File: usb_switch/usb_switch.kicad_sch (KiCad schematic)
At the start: 79 parts, among them J1 Jack-DC, J2 USB_B_Micro, J3 Conn_01x04, J4 USB_A, J5 USB_A, J6 USB_A, J7 USB_A, J8 UART, U1 AMS1117-3.3, U2 USB2514B_Bi, U3 MIC2026-1BM, U4 MIC2026-1BM, U5 MCP2221-I_SL, Y1 24MHz

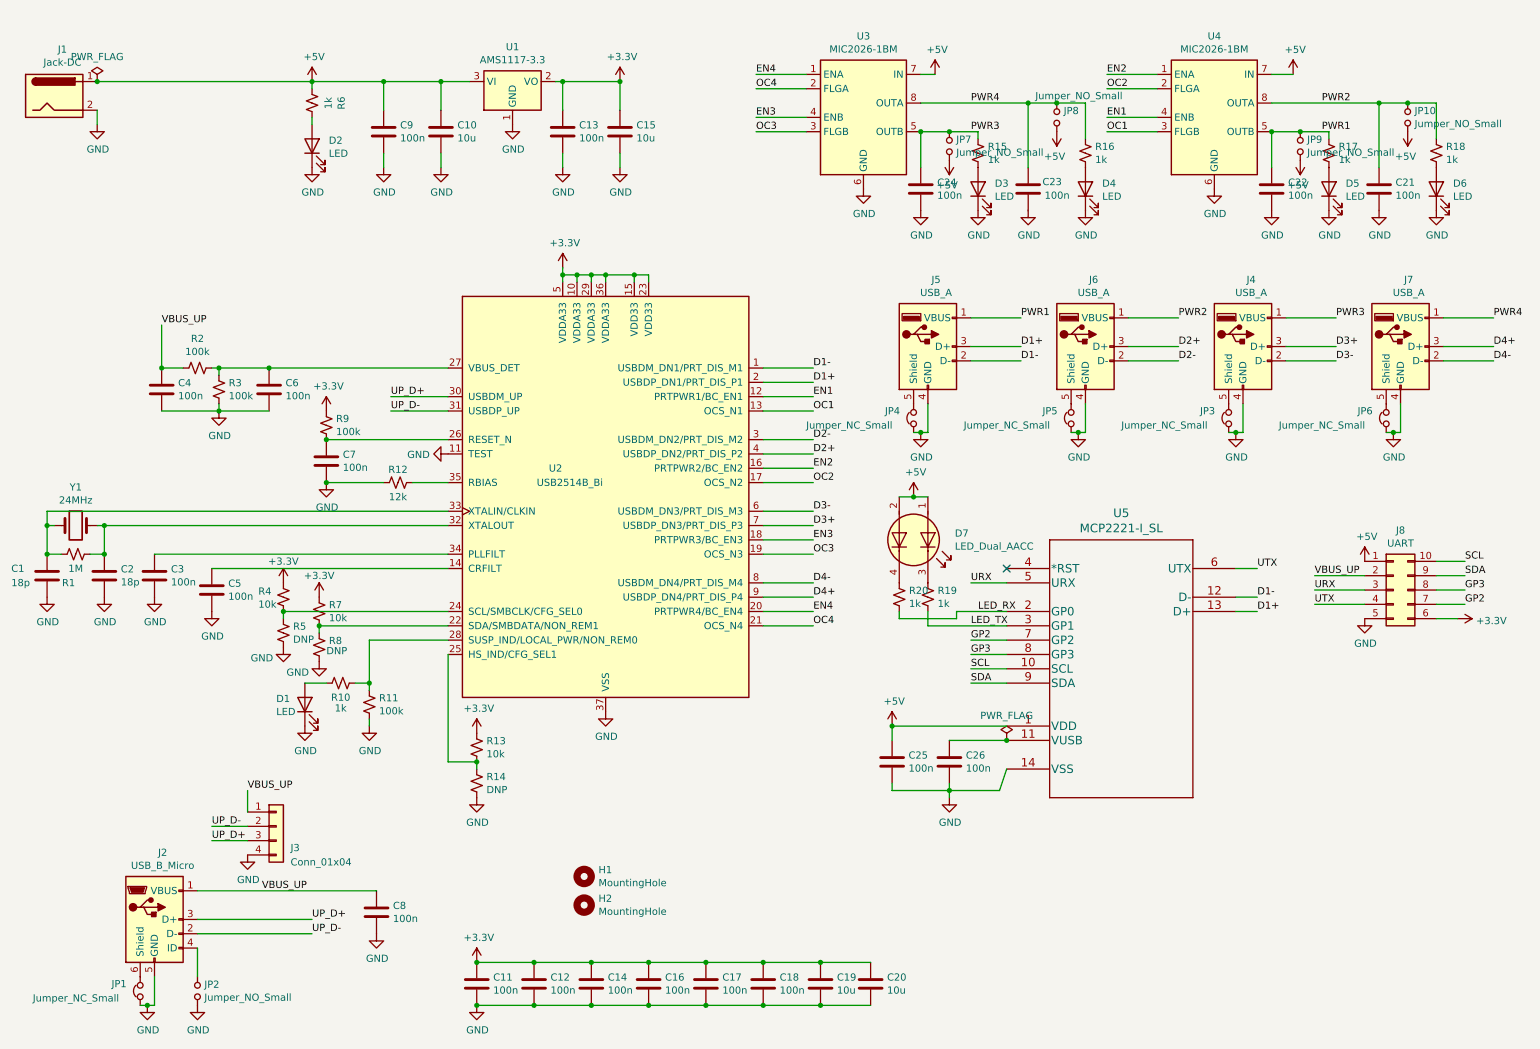
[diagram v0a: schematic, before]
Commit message: Slide switch library
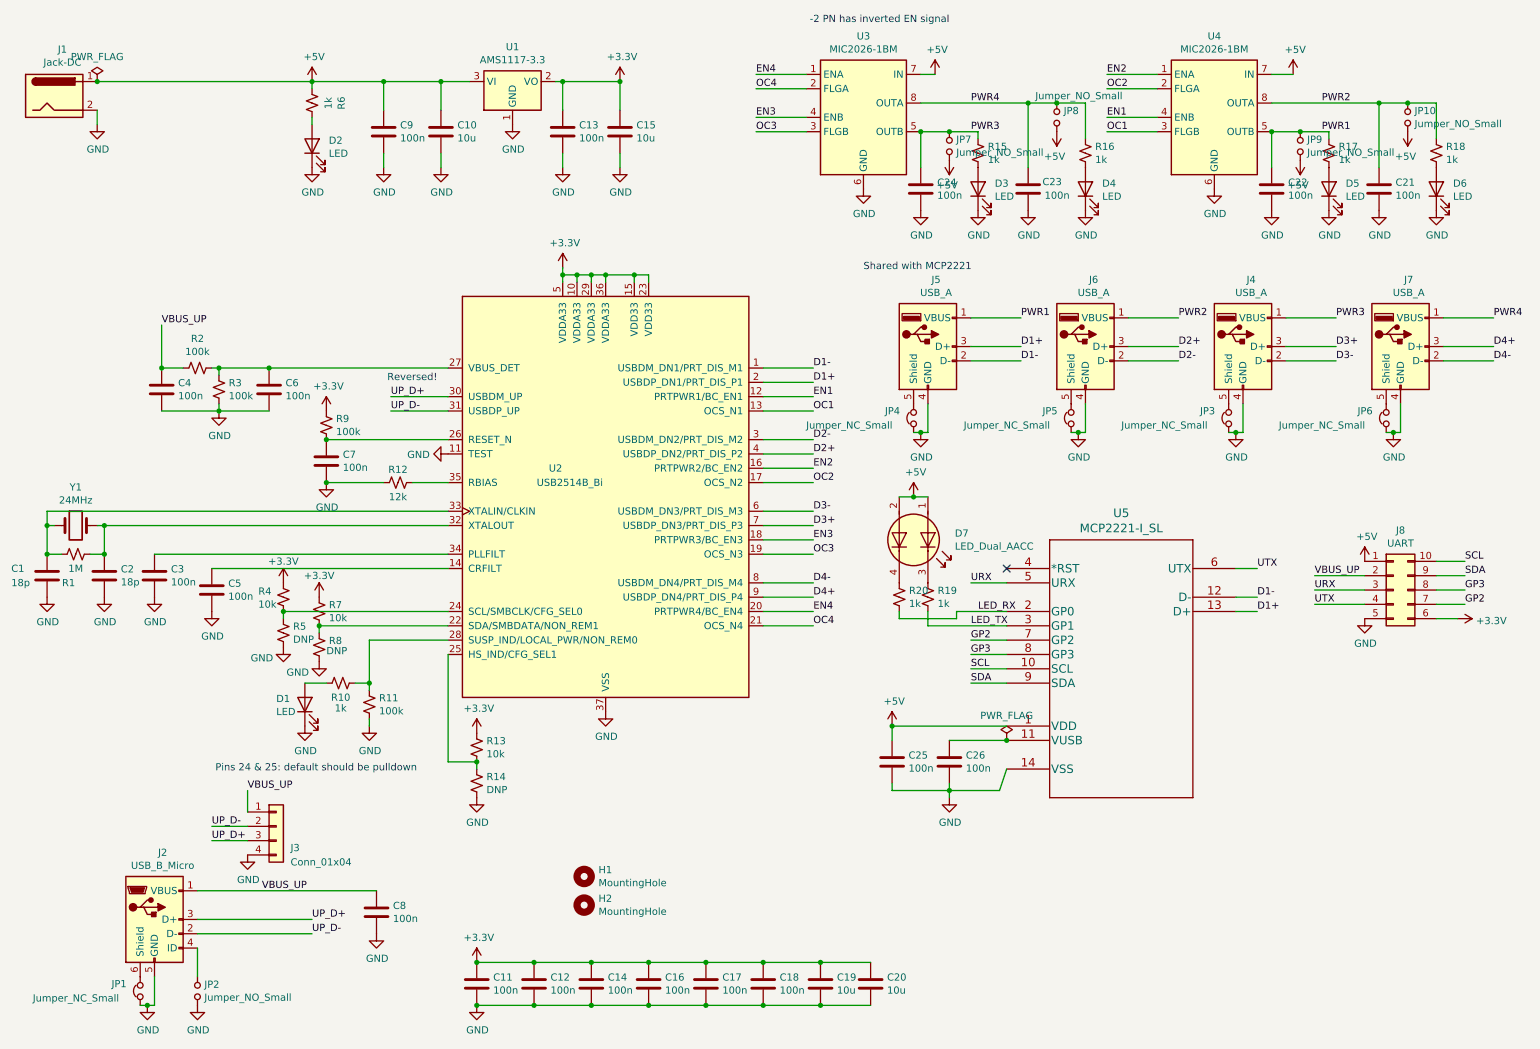
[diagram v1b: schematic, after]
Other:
- note added: "-2 PN has inverted EN signal"
- note added: "Pins 24 & 25: default should be pulldown"
- note added: "Reversed!"
- note added: "Shared with MCP2221"
